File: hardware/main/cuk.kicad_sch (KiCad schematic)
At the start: 58 parts, among them Q401 BSC093N15NS5, Q402 BSC093N15NS5

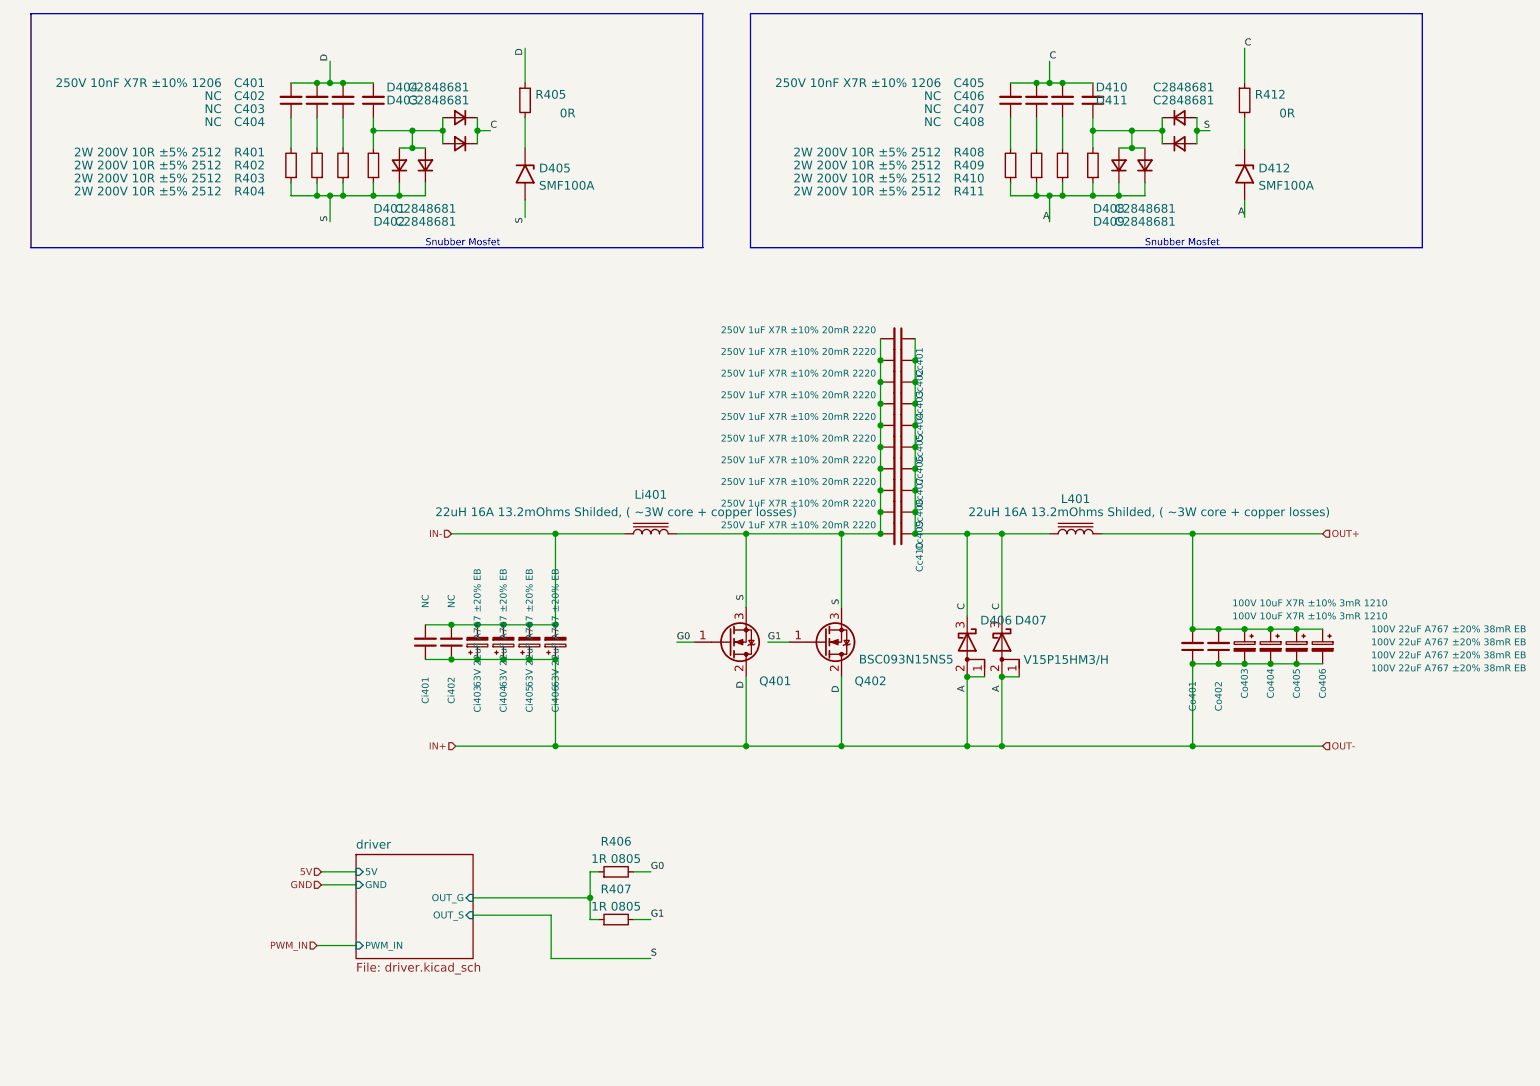
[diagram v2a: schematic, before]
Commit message: Schematics: Run DRC and fix errors and some warnings, also added Zenite kicad library repo as submodule
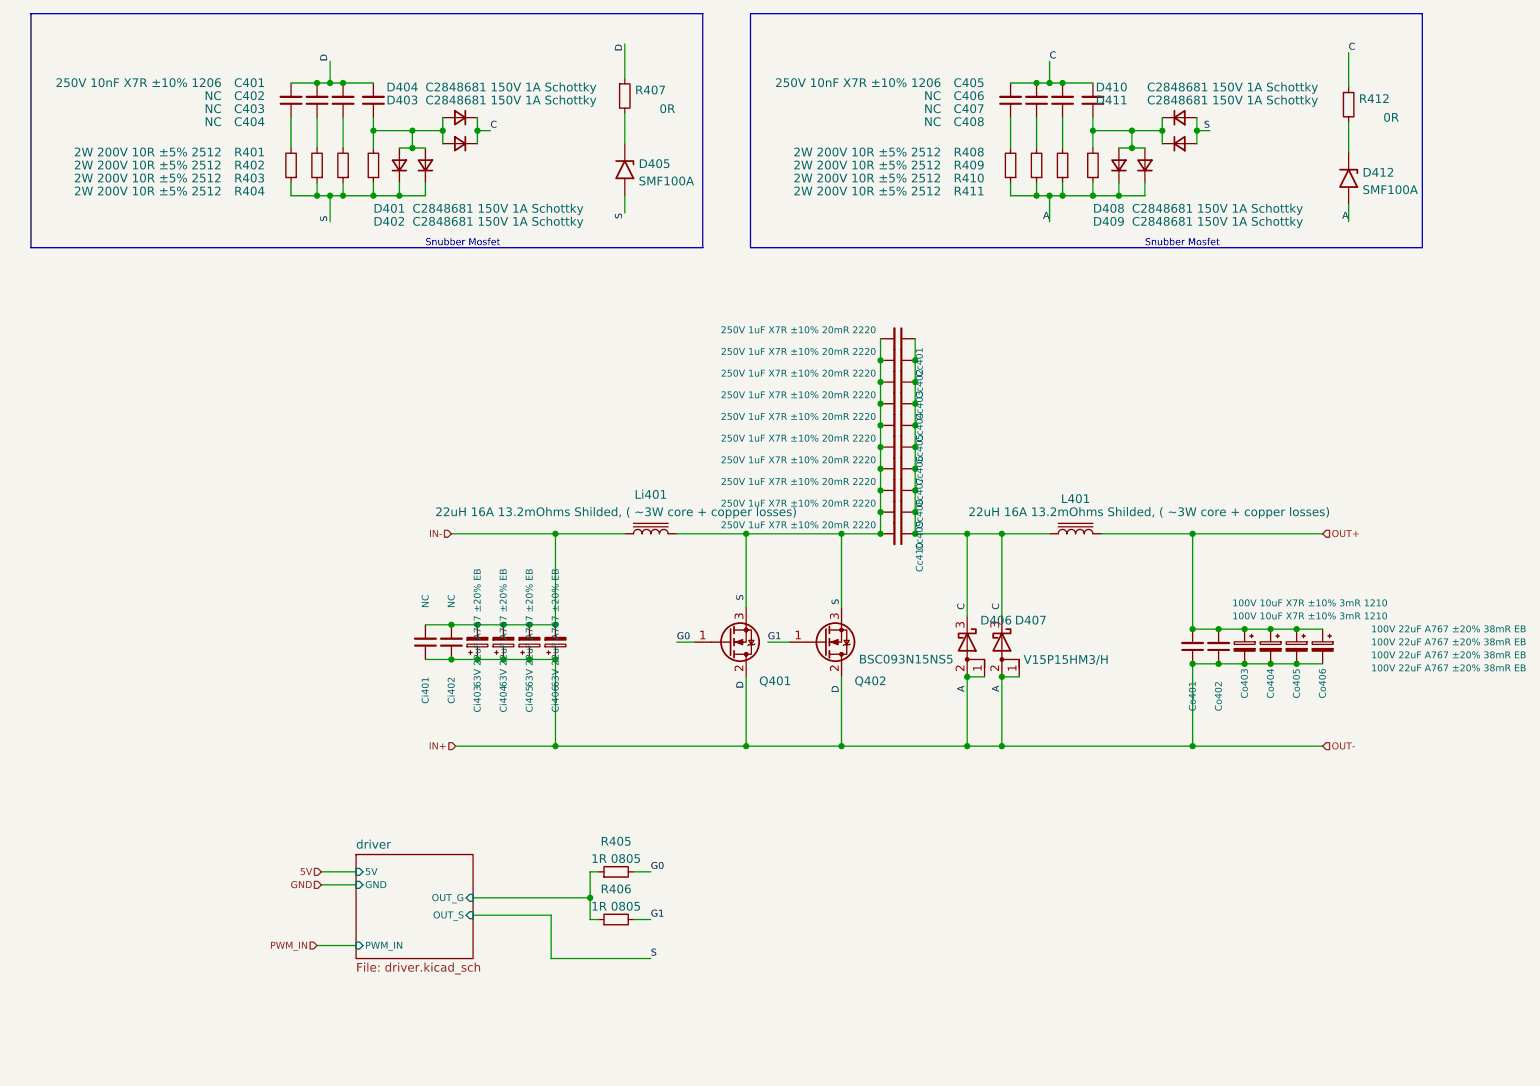
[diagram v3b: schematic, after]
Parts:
- C401, C402, C403, C404, C405, C406, C407, C408: footprint (none) -> Capacitor_SMD:C_1206_3216Metric_Pad1.33x1.80mm_HandSolder
- Cc401, Cc402, Cc403, Cc404, Cc405, Cc406, Cc407, Cc408, Cc409, Cc410: footprint (none) -> Capacitor_SMD:C_2220_5650Metric
- Ci401, Ci402, Co401, Co402: footprint (none) -> Capacitor_SMD:C_1210_3225Metric
- Ci403, Ci404, Ci405, Ci406, Co403, Co404, Co405, Co406: footprint (none) -> Capacitor_SMD:CP_Elec_8x6.7
- D401, D402, D403, D404, D408, D409, D410, D411: value C2848681 -> C2848681 150V 1A Schottky; footprint (none) -> Diode_SMD:D_SMA_Handsoldering
- L401, Li401: footprint (none) -> Zenite:L_Pulse_PM227
- Q401, Q402: footprint Zenite:PG-TDSON-8-FL -> Zenite:TDSON-8-3
- R401, R402, R403, R404, R408, R409, R410, R411: footprint (none) -> Resistor_SMD:R_2512_6332Metric_Pad1.40x3.35mm_HandSolder
- R405: renamed from R406; footprint (none) -> Resistor_SMD:R_0805_2012Metric_Pad1.20x1.40mm_HandSolder
- R406: renamed from R407; footprint (none) -> Resistor_SMD:R_0805_2012Metric_Pad1.20x1.40mm_HandSolder
- R407: renamed from R405; footprint (none) -> Resistor_SMD:R_0805_2012Metric_Pad1.20x1.40mm_HandSolder
- R412: footprint (none) -> Resistor_SMD:R_0805_2012Metric_Pad1.20x1.40mm_HandSolder
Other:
- moved on the sheet: D405, D412, R407, R412

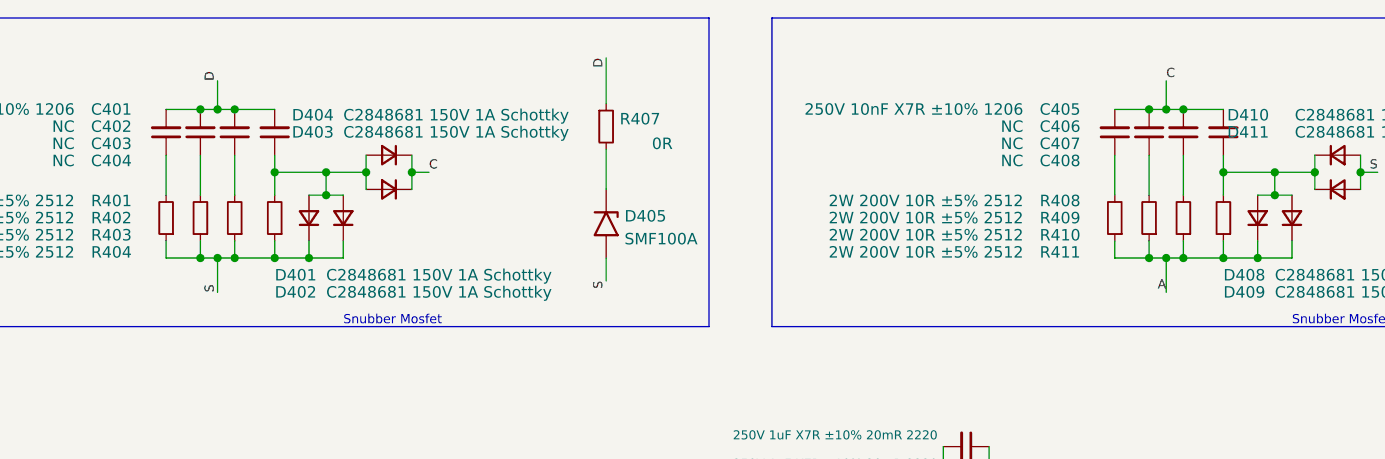
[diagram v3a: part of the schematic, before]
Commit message: Layout: Organizing components
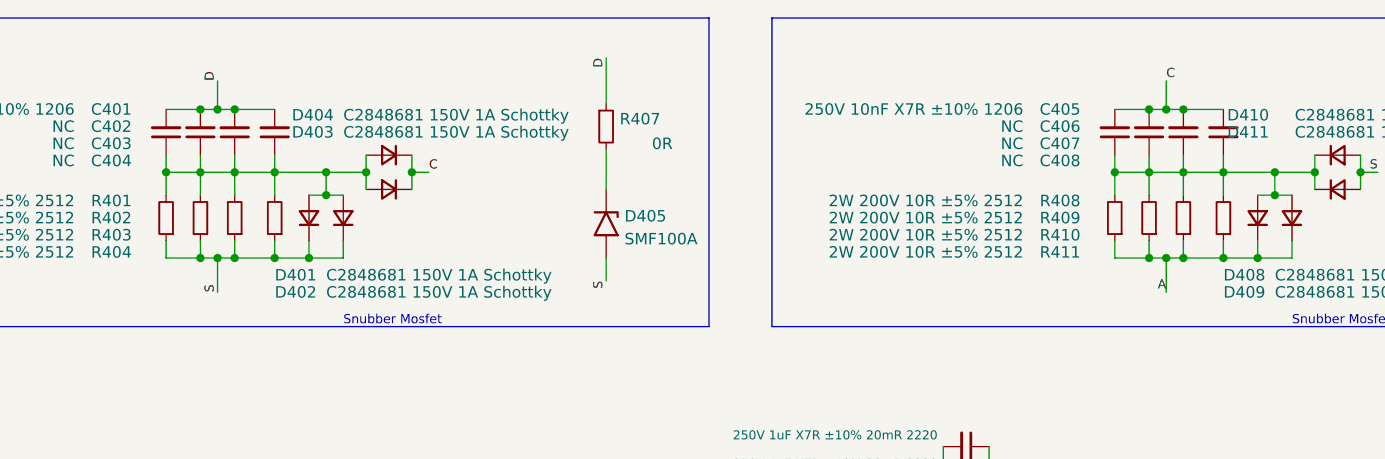
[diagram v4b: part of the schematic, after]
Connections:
- net at C402.1, R402.2: now also C401.1, C403.1, C404.1, D401.2 (A), D402.2 (A), D403.2 (A), D404.2 (A), R401.2, R403.2, R404.2
- net at C407.1, R410.2: now also C405.1, C406.1, C408.1, D408.2 (A), D409.2 (A), D410.1 (K), D411.1 (K), R408.2, R409.2, R411.2
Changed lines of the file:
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@@
   (junction (at 159.385 100.33) (diameter 0) (color 0 0 0 0)
   )
+  (junction (at 169.545 41.275) (diameter 0) (color 0 0 0 0)
+  )
   (junction (at 104.14 153.67) (diameter 0) (color 0 0 0 0)
   )
@@
   (junction (at 95.25 118.745) (diameter 0) (color 0 0 0 0)
   )
+  (junction (at 67.945 41.275) (diameter 0) (color 0 0 0 0)
+  )
   (junction (at 207.645 114.3) (diameter 0) (color 0 0 0 0)
   )
@@
   (junction (at 146.685 97.155) (diameter 0) (color 0 0 0 0)
   )
+  (junction (at 60.325 41.275) (diameter 0) (color 0 0 0 0)
+  )
   (junction (at 207.645 119.38) (diameter 0) (color 0 0 0 0)
   )
@@
   (junction (at 164.465 121.285) (diameter 0) (color 0 0 0 0)
   )
+  (junction (at 165.735 41.275) (diameter 0) (color 0 0 0 0)
+  )
   (junction (at 151.765 74.93) (diameter 0) (color 0 0 0 0)
   )
@@
   (junction (at 66.04 34.29) (diameter 0) (color 0 0 0 0)
   )
+  (junction (at 173.355 41.275) (diameter 0) (color 0 0 0 0)
+  )
   (junction (at 67.945 34.29) (diameter 0) (color 0 0 0 0)
   )
@@
   (junction (at 159.385 121.285) (diameter 0) (color 0 0 0 0)
   )
+  (junction (at 64.135 41.275) (diameter 0) (color 0 0 0 0)
+  )
   (junction (at 64.135 34.29) (diameter 0) (color 0 0 0 0)
   )
@@
     (stroke (width 0) (type default) (color 0 0 0 0))
   )
+  (wire (pts (xy 64.135 41.275) (xy 67.945 41.275))
+    (stroke (width 0) (type default) (color 0 0 0 0))
+  )
   (wire (pts (xy 181.61 43.815) (xy 183.515 43.815))
     (stroke (width 0) (type default) (color 0 0 0 0))
@@
     (stroke (width 0) (type default) (color 0 0 0 0))
   )
-  (wire (pts (xy 173.355 43.815) (xy 173.355 39.37))
+  (wire (pts (xy 173.355 43.815) (xy 173.355 41.275))
     (stroke (width 0) (type default) (color 0 0 0 0))
   )
@@
     (stroke (width 0) (type default) (color 0 0 0 0))
   )
-  (wire (pts (xy 165.735 43.815) (xy 165.735 39.37))
+  (wire (pts (xy 165.735 43.815) (xy 165.735 41.275))
     (stroke (width 0) (type default) (color 0 0 0 0))
   )
@@
     (stroke (width 0) (type default) (color 0 0 0 0))
   )
-  (wire (pts (xy 60.325 43.815) (xy 60.325 39.37))
+  (wire (pts (xy 60.325 43.815) (xy 60.325 41.275))
     (stroke (width 0) (type default) (color 0 0 0 0))
   )
@@
     (stroke (width 0) (type default) (color 0 0 0 0))
   )
+  (wire (pts (xy 173.355 41.275) (xy 173.355 39.37))
+    (stroke (width 0) (type default) (color 0 0 0 0))
+  )
   (wire (pts (xy 177.8 34.29) (xy 173.355 34.29))
     (stroke (width 0) (type default) (color 0 0 0 0))
@@
     (stroke (width 0) (type default) (color 0 0 0 0))
   )
+  (wire (pts (xy 169.545 41.275) (xy 169.545 39.37))
+    (stroke (width 0) (type default) (color 0 0 0 0))
+  )
   (wire (pts (xy 164.465 121.285) (xy 167.005 121.285))
     (stroke (width 0) (type default) (color 0 0 0 0))
@@
     (stroke (width 0) (type default) (color 0 0 0 0))
   )
-  (wire (pts (xy 67.945 43.815) (xy 67.945 39.37))
+  (wire (pts (xy 67.945 43.815) (xy 67.945 41.275))
     (stroke (width 0) (type default) (color 0 0 0 0))
   )
@@
     (stroke (width 0) (type default) (color 0 0 0 0))
   )
+  (wire (pts (xy 60.325 41.275) (xy 60.325 39.37))
+    (stroke (width 0) (type default) (color 0 0 0 0))
+  )
+  (wire (pts (xy 165.735 41.275) (xy 169.545 41.275))
+    (stroke (width 0) (type default) (color 0 0 0 0))
+  )
   (wire (pts (xy 146.685 93.98) (xy 146.685 97.155))
     (stroke (width 0) (type default) (color 0 0 0 0))
@@
     (stroke (width 0) (type default) (color 0 0 0 0))
   )
+  (wire (pts (xy 64.135 41.275) (xy 64.135 39.37))
+    (stroke (width 0) (type default) (color 0 0 0 0))
+  )
   (wire (pts (xy 76.2 50.8) (xy 80.01 50.8))
     (stroke (width 0) (type default) (color 0 0 0 0))
@@
     (stroke (width 0) (type default) (color 0 0 0 0))
   )
+  (wire (pts (xy 67.945 41.275) (xy 67.945 39.37))
+    (stroke (width 0) (type default) (color 0 0 0 0))
+  )
   (wire (pts (xy 84.455 131.445) (xy 99.06 131.445))
     (stroke (width 0) (type default) (color 0 0 0 0))
@@
     (stroke (width 0) (type default) (color 0 0 0 0))
   )
-  (wire (pts (xy 64.135 43.815) (xy 64.135 39.37))
+  (wire (pts (xy 173.355 41.275) (xy 177.8 41.275))
+    (stroke (width 0) (type default) (color 0 0 0 0))
+  )
+  (wire (pts (xy 64.135 43.815) (xy 64.135 41.275))
     (stroke (width 0) (type default) (color 0 0 0 0))
   )
@@
     (stroke (width 0) (type default) (color 0 0 0 0))
   )
-  (wire (pts (xy 169.545 43.815) (xy 169.545 39.37))
+  (wire (pts (xy 67.945 41.275) (xy 72.39 41.275))
+    (stroke (width 0) (type default) (color 0 0 0 0))
+  )
+  (wire (pts (xy 169.545 43.815) (xy 169.545 41.275))
     (stroke (width 0) (type default) (color 0 0 0 0))
   )
@@
     (stroke (width 0) (type default) (color 0 0 0 0))
   )
+  (wire (pts (xy 165.735 41.275) (xy 165.735 39.37))
+    (stroke (width 0) (type default) (color 0 0 0 0))
+  )
   (wire (pts (xy 146.685 84.455) (xy 146.685 87.63))
     (stroke (width 0) (type default) (color 0 0 0 0))
@@
     (stroke (width 0) (type default) (color 0 0 0 0))
   )
+  (wire (pts (xy 60.325 41.275) (xy 64.135 41.275))
+    (stroke (width 0) (type default) (color 0 0 0 0))
+  )
+  (wire (pts (xy 169.545 41.275) (xy 173.355 41.275))
+    (stroke (width 0) (type default) (color 0 0 0 0))
+  )

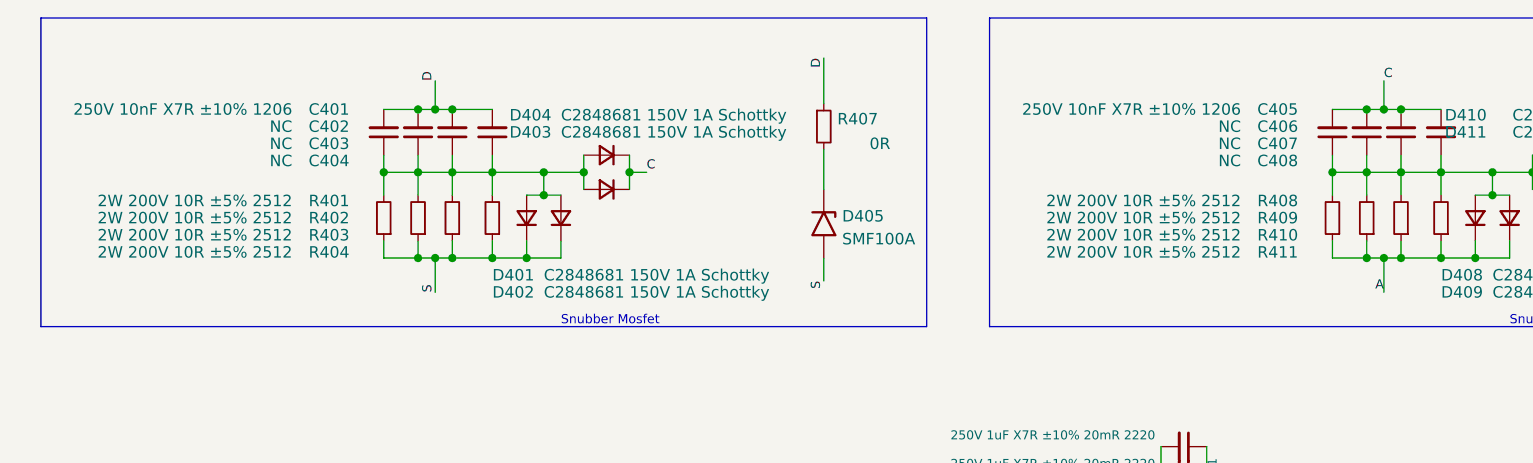
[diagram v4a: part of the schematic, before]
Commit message: Layout: Organizing power components
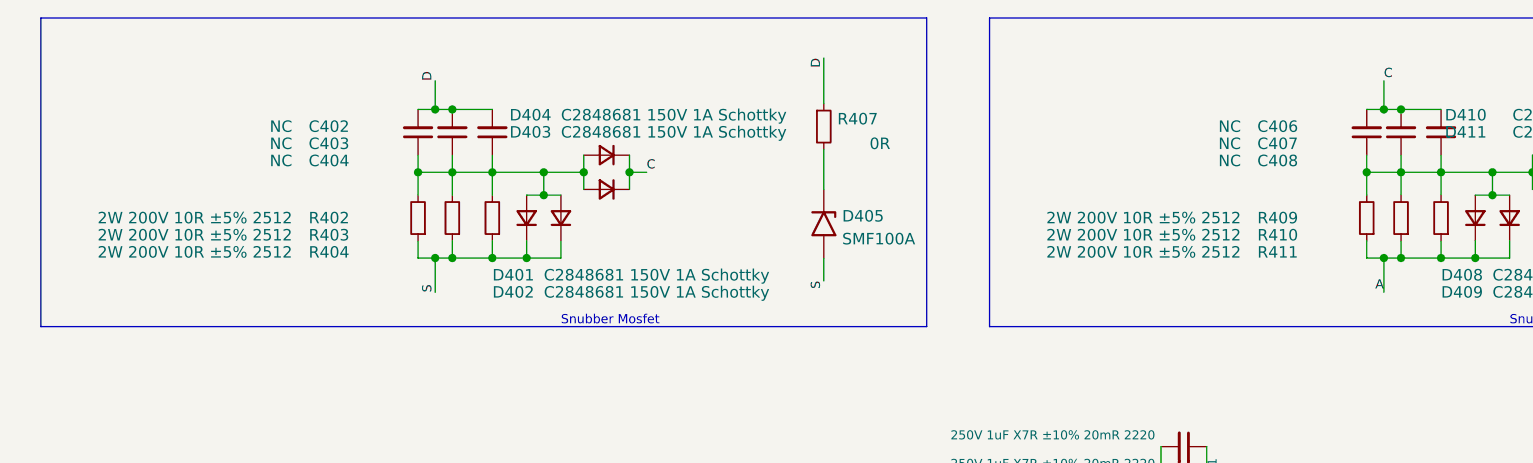
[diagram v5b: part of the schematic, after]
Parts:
- removed C401, C405: 250V 10nF X7R ±10% 1206, Capacitor_SMD:C_1206_3216Metric_Pad1.33x1.80mm_HandSolder, symbol Device:C_Small
- removed R401, R408: 2W 200V 10R ±5% 2512, Resistor_SMD:R_2512_6332Metric_Pad1.40x3.35mm_HandSolder, symbol Device:R_Small
- Ci403, Ci404, Ci405, Ci406: footprint Capacitor_SMD:CP_Elec_8x6.7 -> Capacitor_SMD:CP_Elec_8x10
- Co403, Co404, Co405, Co406: footprint Capacitor_SMD:CP_Elec_8x6.7 -> Capacitor_SMD:CP_Elec_10x12.5
- D401, D402, D403, D404, D408, D409, D410, D411: footprint Diode_SMD:D_SMA_Handsoldering -> Diode_SMD:D_SMA
